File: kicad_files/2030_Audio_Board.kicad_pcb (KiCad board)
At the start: 2 copper layers, 50 x 50 mm, 19 parts, among them U1 TDA2030

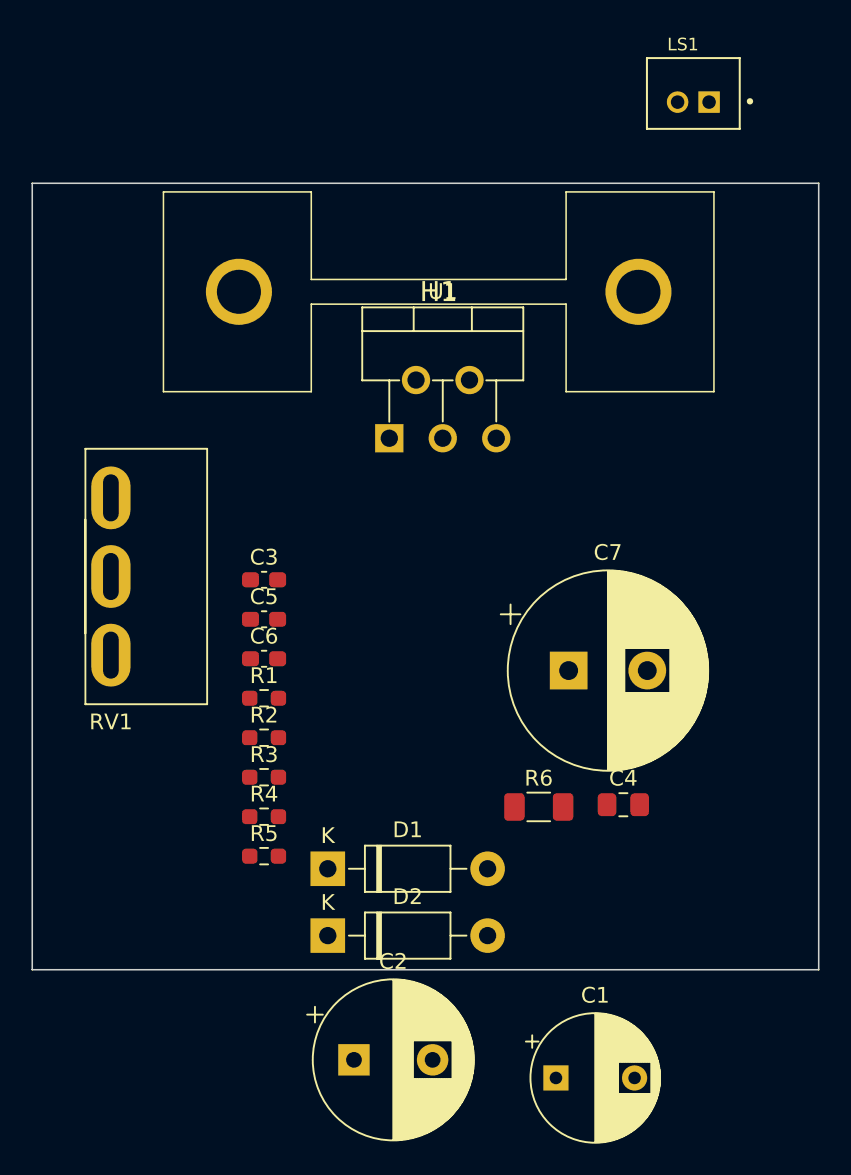
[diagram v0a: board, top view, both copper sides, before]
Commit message: routing completed in single layer
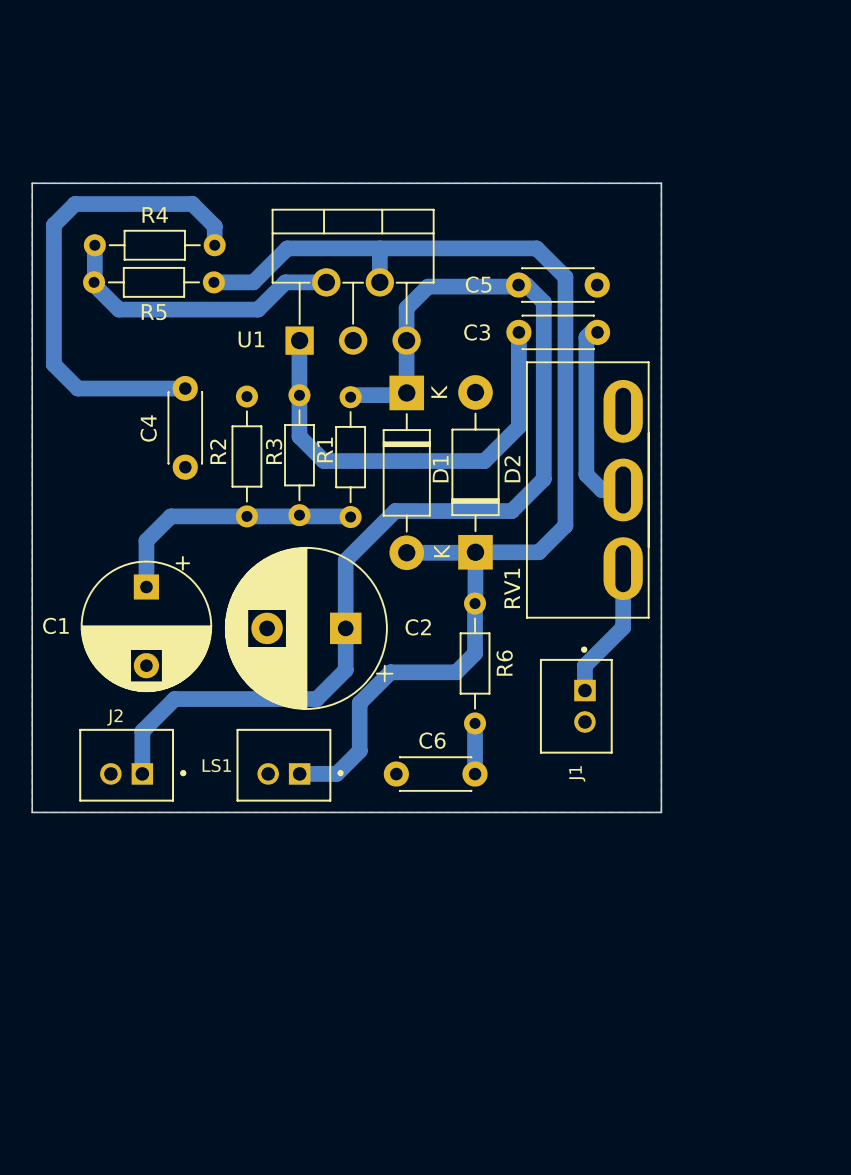
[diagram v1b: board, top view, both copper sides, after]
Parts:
- removed C7: 2000uf, Capacitor_THT:CP_Radial_D12.5mm_P5.00mm
- removed H1: HSE-B20254-035H-01, SamacSys_Parts:HSEB20254035H01
- added J1: Conn_01x02_Pin, footprints:JST_B2B-PH-K-S(LF)(SN), F.Cu at (134.6, 133.2)
- added J2: Conn_01x02_Pin, footprints:JST_B2B-PH-K-S(LF)(SN), F.Cu at (106.0, 137.0)
- C3, C5, C6: footprint Capacitor_SMD:C_0603_1608Metric_Pad1.08x0.95mm_HandSolder -> Capacitor_THT:C_Disc_D4.3mm_W1.9mm_P5.00mm
- C4: footprint Capacitor_SMD:C_0805_2012Metric_Pad1.18x1.45mm_HandSolder -> Capacitor_THT:C_Disc_D4.3mm_W1.9mm_P5.00mm
- R1, R2, R3, R4, R5: footprint Resistor_SMD:R_0603_1608Metric_Pad0.98x0.95mm_HandSolder -> Resistor_THT:R_Axial_DIN0204_L3.6mm_D1.6mm_P7.62mm_Horizontal
- R6: footprint Resistor_SMD:R_1206_3216Metric_Pad1.30x1.75mm_HandSolder -> Resistor_THT:R_Axial_DIN0204_L3.6mm_D1.6mm_P7.62mm_Horizontal
- moved LS1 50.0 mm to (116.0, 137.0)
- moved C1 40.6 mm to (107.3, 125.7), turned to -90 degrees
- moved C4 38.4 mm to (109.7, 113.0), turned to -90 degrees
- moved R5 36.6 mm to (111.5, 106.3), turned to 180 degrees
- moved R4 36.5 mm to (111.6, 103.9), turned to 180 degrees
- moved RV1 32.9 mm to (137.6, 124.5), turned to 0 degrees
- moved D1 30.7 mm to (123.8, 113.3), turned to -90 degrees
- moved C2 27.4 mm to (119.9, 128.3), turned to 180 degrees
- moved C5 26.7 mm to (130.9, 106.5)
- moved C3 26.4 mm to (135.9, 109.5), turned to 180 degrees
- moved D2 26.1 mm to (128.2, 123.5), turned to 90 degrees
- moved R2 21.7 mm to (113.7, 113.6), turned to -90 degrees
- moved R3 16.8 mm to (117.0, 121.1), turned to 90 degrees
- moved C6 15.3 mm to (128.2, 137.6), turned to 180 degrees
- moved R6 13.5 mm to (128.2, 126.7), turned to -90 degrees
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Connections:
- C1 pad 2: -12V -> GND
- C2 pad 2: -12V -> GND
- C4 pad 2: -12V -> GND
- C5 pad 2: -12V -> GND
- C6 pad 2: -12V -> GND
- D2 pad 2: -12V -> GND
- LS1 pad 1: Net-(C7-Pad2) -> Net-(D1-A)
- LS1 pad 2: -12V -> GND
- R2 pad 1: -12V -> GND
- U1 pad 3: -12V -> GND
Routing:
- net Net-(D1-A): track 0.00 -> 75.3 mm
- net +12V: track 0.00 -> 69.0 mm
- net Net-(C4-Pad1): track 0.00 -> 30.4 mm
- net Net-(U1-+): track 0.00 -> 27.6 mm
- net Net-(U1--): track 0.00 -> 18.6 mm
- net Net-(C1-Pad1): track 0.00 -> 16.6 mm
- net Net-(C3-Pad1): track 0.00 -> 12.3 mm
- net Signal_INPUT: track 0.00 -> 8.76 mm
- net Net-(C6-Pad1): track 0.00 -> 3.22 mm
- added copper zone on B.Cu, net GND
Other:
- board size 50 x 50 mm -> 40 x 40 mm
